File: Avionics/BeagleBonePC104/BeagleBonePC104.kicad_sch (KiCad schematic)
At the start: 0 parts

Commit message: Ian Goldberg - finished the pc104 pinout for the beaglebone motherboard
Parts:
- added U1: ~, symbol BeagleBoneBlackPinout:BeagleBoneBlackPinout
- added U2: ~, symbol PCI104:PCI104Connector
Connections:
- new net GND: U1.1 (GND), U1.2 (GND)
- new net UART5_RX: U2.35 (PLOD_STAT_3)
- new net UART5_TX: U2.33 (PLOD_STAT_1)

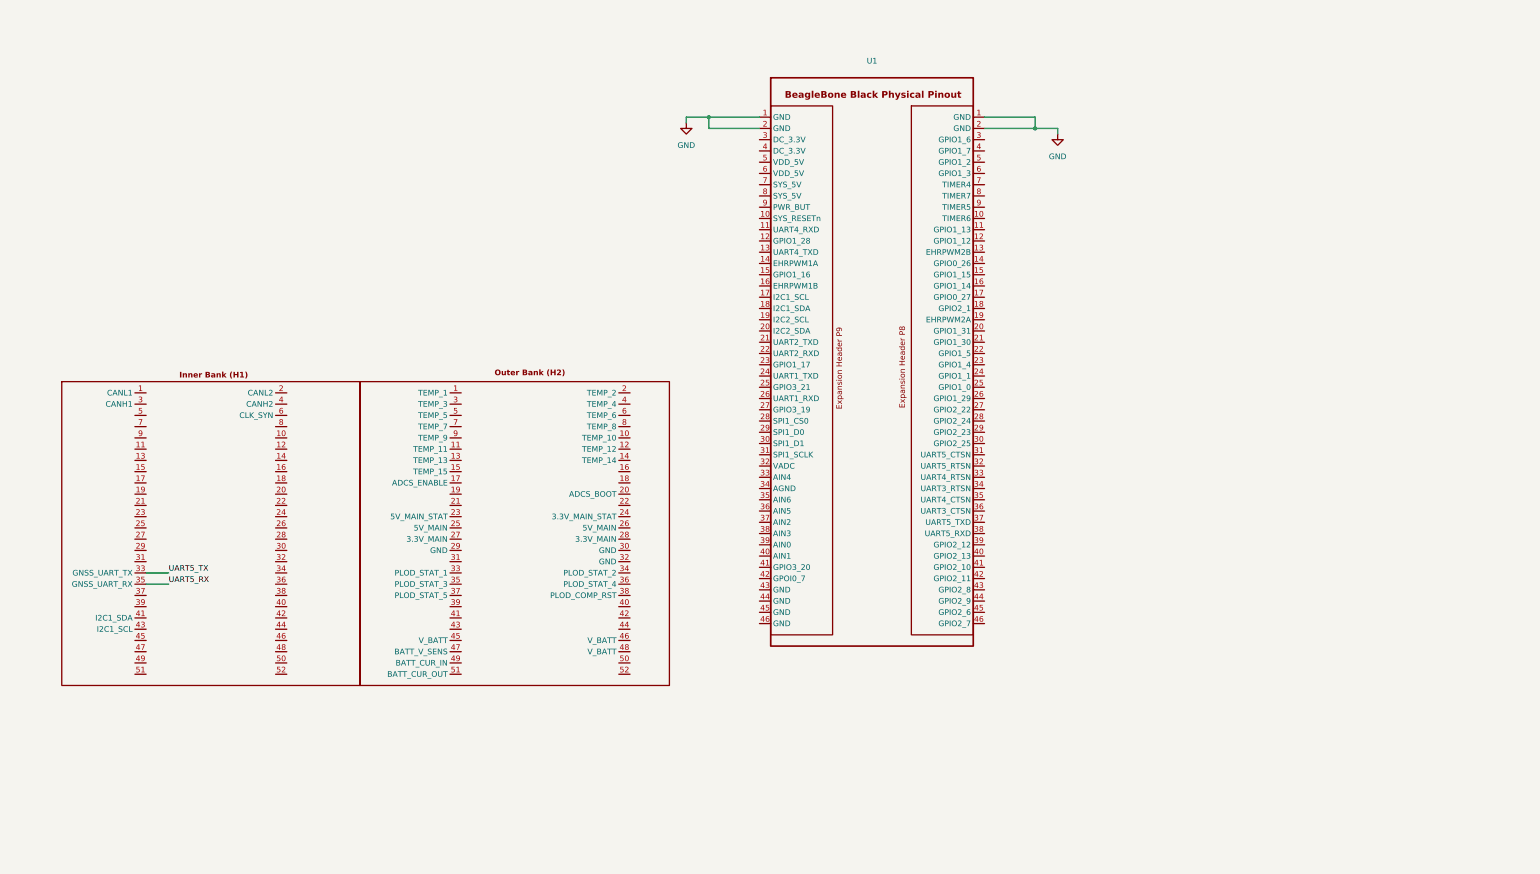
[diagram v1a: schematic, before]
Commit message: Ian Goldberg - Made more changes to the pc104 header for the BeagleBone
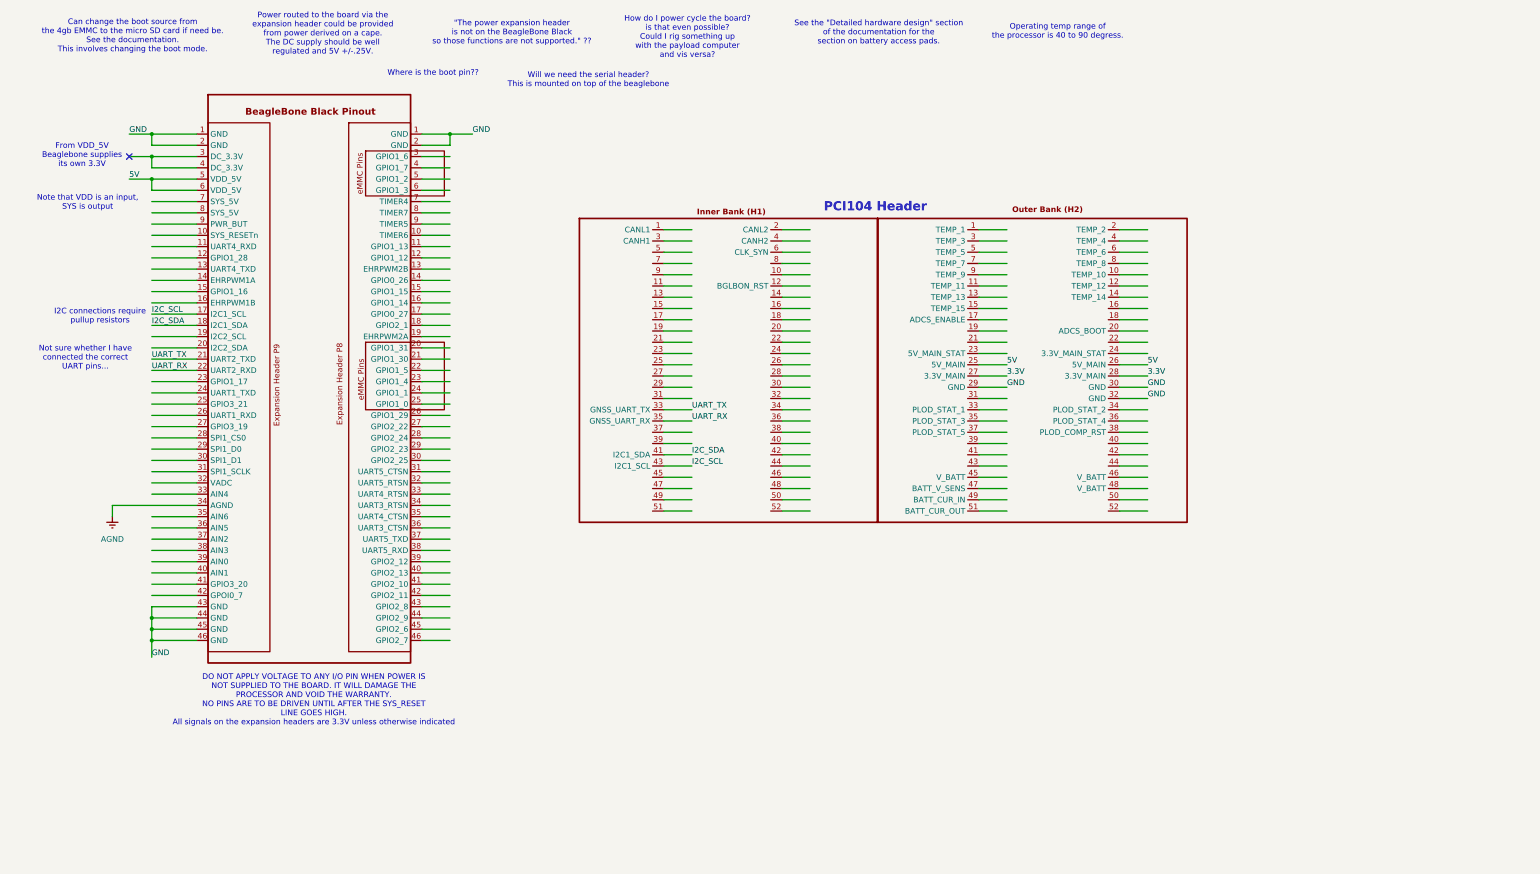
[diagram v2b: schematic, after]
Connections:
- net UART5_RX is gone; now on net UART_RX: U2.35 (PLOD_STAT_3)
- net UART5_TX is gone; now on net UART_TX: U2.33 (PLOD_STAT_1)
- net GND: now also U1.43 (GPIO2_8), U1.44 (GPIO2_9), U1.45 (GPIO2_6), U1.46 (GPIO2_7), U2.29 (GND), U2.30 (GND), U2.32 (GND)
- net I2C_SCL: now reaches U1.17 (I2C1_SCL)
- net I2C_SCL: now also U2.43 (I2C1_SCL)
- net I2C_SDA: now reaches U1.18 (I2C1_SDA)
- net I2C_SDA: now also U2.41 (I2C1_SDA)
- net UART_TX: now reaches U1.21 (UART2_TXD)
- net UART_RX: now reaches U1.22 (UART2_RXD)
- net at U1.3 (GPIO1_6): now also U1.4 (GPIO1_7)
- net AGND: now reaches U1.34 (UART3_RTSN)
- net 5V: now reaches U1.5 (VDD_5V)
- net 5V: now also U1.6 (VDD_5V), U2.25 (5V_MAIN), U2.26 (5V_MAIN)
- net 3.3V: now reaches U2.27 (3.3V_MAIN)
- net 3.3V: now also U2.28 (3.3V_MAIN)
- no-connect marks 0 -> 1
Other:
- note added: ""The power expansion header is not on the BeagleBone Black so those functions are not supported." ??"
- note added: "Can change the boot source from the 4gb EMMC to the micro SD card if need be. See the documentation. This involves changing the boot mode."
- note added: "DO NOT APPLY VOLTAGE TO ANY I/O PIN WHEN POWER IS NOT SUPPLIED TO THE BOARD. IT WILL DAMAGE THE PROCESSOR AND VOID THE WARRANTY. NO PINS ARE TO BE DRIVEN UNTIL AFTER THE SYS_RESET LINE GOES HIGH. All signals on the expansion headers are 3.3V unless otherwise indicated"
- note added: "From VDD_5V Beaglebone supplies its own 3.3V"
- note added: "How do I power cycle the board? is that even possible? Could I rig something up with the payload computer and vis versa?"
- note added: "I2C connections require pullup resistors"
- note added: "Not sure whether I have connected the correct UART pins..."
- note added: "Note that VDD is an input, SYS is output"
- note added: "Operating temp range of the processor is 40 to 90 degress."
- note added: "PCI104 Header"
- note added: "Power routed to the board via the expansion header could be provided from power derived on a cape. The DC supply should be well regulated and 5V +/-.25V."
- note added: "See the "Detailed hardware design" section of the documentation for the section on battery access pads."
- note added: "Where is the boot pin??"
- note added: "Will we need the serial header? This is mounted on top of the beaglebone"

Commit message: Ian Goldberg - Finished the pc104 pinout for the beaglebone motherboard
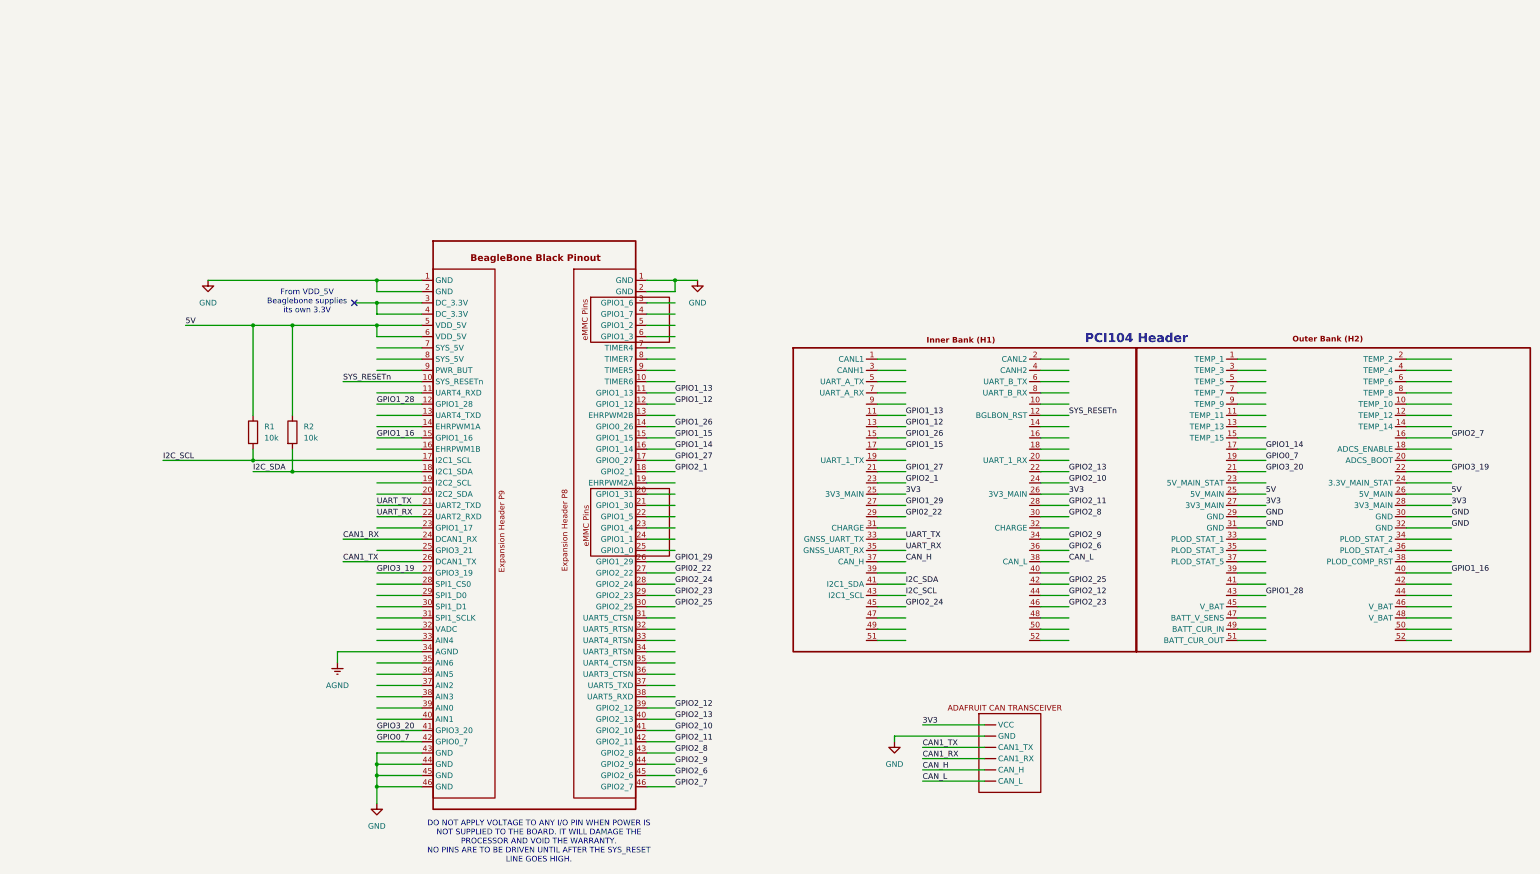
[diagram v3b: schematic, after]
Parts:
- added R1, R2: 10k, symbol Device:R
- added U3: ~, symbol BeagleBoneBlackPinout:AdafruitCANTransciever
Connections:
- net 5V: now also R1.1, R2.1
- net GND: now also U2.31 (GND), U3. (VCC)
- net I2C_SCL: now also R1.2
- net I2C_SDA: now also R2.2
- net SYS_RESETn: now reaches U1.10 (TIMER6)
- net SYS_RESETn: now also U2.12 (TEMP_12)
- net GPIO1_13: now reaches U1.11 (UART4_RXD)
- net GPIO1_13: now also U2.11 (TEMP_11)
- net GPIO1_28: now reaches U1.12 (GPIO1_28)
- net GPIO1_28: now also U2.43 (I2C1_SCL)
- net GPIO1_26: now reaches U1.14 (GPIO0_26)
- net GPIO1_26: now also U2.15 (TEMP_15)
- net GPIO1_16: now reaches U1.15 (GPIO1_16)
- net GPIO1_16: now also U2.40
- net GPIO1_14: now reaches U1.16 (GPIO1_14)
- net GPIO1_14: now also U2.17
- net CAN1_RX: now reaches U1.24 (GPIO1_1)
- net CAN1_RX: now also U3. (VCC)
- net GPIO1_29: now reaches U1.26 (GPIO1_29)
- net GPIO1_29: now also U2.27 (3V3_MAIN)
- net GPIO3_19: now reaches U1.27 (GPIO3_19)
- net GPIO3_19: now also U2.22
- net GPIO2_24: now reaches U1.28 (SPI1_CS0)
- net GPIO2_24: now also U2.45 (V_BAT)
- net GPIO2_23: now reaches U1.29 (SPI1_D0)
- net GPIO2_23: now also U2.46 (V_BAT)
- net at U1.3 (GPIO1_6): now also U1.4 (GPIO1_7)
- net at U1.4 (GPIO1_7): no longer U1.3 (GPIO1_6)
- net GPIO2_25: now reaches U1.30 (SPI1_D1)
- net GPIO2_25: now also U2.42
- net GPIO2_12: now reaches U1.39 (GPIO2_12)
- net GPIO2_12: now also U2.44
- net GPIO2_13: now reaches U1.40 (GPIO2_13)
- net GPIO2_13: now also U2.22
- net GPIO3_20: now reaches U1.41 (GPIO3_20)
- net GPIO3_20: now also U2.21
- net GPIO2_11: now reaches U1.42 (GPIO2_11)
- net GPIO2_11: now also U2.28 (3V3_MAIN)
- net GPIO2_8: now reaches U1.43 (GPIO2_8)
- net GPIO2_8: now also U2.30 (GND)
- net GPIO2_9: now reaches U1.44 (GPIO2_9)
- net GPIO2_9: now also U2.34 (PLOD_STAT_2)
- net GPIO2_6: now reaches U1.45 (GPIO2_6)
- net GPIO2_6: now also U2.36 (PLOD_STAT_4)
- net GPIO2_7: now reaches U1.46 (GPIO2_7)
- net GPIO2_7: now also U2.16
- net GPIO1_12: now reaches U2.13 (TEMP_13)
- net GPIO1_12: now also U1.12 (GPIO1_28)
- net GPIO1_15: now reaches U2.17
- net GPIO1_15: now also U1.15 (GPIO1_16)
- net GPIO0_7: now reaches U2.19 (UART_1_TX)
- net GPIO0_7: now also U1.42 (GPIO2_11)
- net GPIO2_1: now reaches U2.23 (5V_MAIN_STAT)
- net GPIO2_1: now also U1.18 (I2C1_SDA)
- net GPIO2_10: now reaches U2.24 (3.3V_MAIN_STAT)
- net GPIO2_10: now also U1.41 (GPIO3_20)
- net GPI02_22: now reaches U2.29 (GND)
- net GPI02_22: now also U1.27 (GPIO3_19)
- net CAN_H: now reaches U2.37 (PLOD_STAT_5)
- net CAN_H: now also U3. (VCC)
- net CAN_L: now reaches U2.38 (PLOD_COMP_RST)
- net CAN_L: now also U3. (VCC)
- removed net 3.3V: U2.27 (3.3V_MAIN), U2.28 (3.3V_MAIN)
- new net 3V3: U2.25 (5V_MAIN), U2.26 (5V_MAIN), U2.27 (3V3_MAIN), U2.28 (3V3_MAIN), U3. (VCC)
- new net CAN1_TX: U1.26 (GPIO1_29), U3. (VCC)
- new net GPIO1_27: U1.17 (I2C1_SCL), U2.21
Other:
- note added: "DO NOT APPLY VOLTAGE TO ANY I/O PIN WHEN POWER IS NOT SUPPLIED TO THE BOARD. IT WILL DAMAGE THE PROCESSOR AND VOID THE WARRANTY. NO PINS ARE TO BE DRIVEN UNTIL AFTER THE SYS_RESET LINE GOES HIGH."
- note removed: ""The power expansion header is not on the BeagleBone Black so those functions are not supported." ??"
- note removed: "Can change the boot source from the 4gb EMMC to the micro SD card if need be. See the documentation. This involves changing the boot mode."
- note removed: "DO NOT APPLY VOLTAGE TO ANY I/O PIN WHEN POWER IS NOT SUPPLIED TO THE BOARD. IT WILL DAMAGE THE PROCESSOR AND VOID THE WARRANTY. NO PINS ARE TO BE DRIVEN UNTIL AFTER THE SYS_RESET LINE GOES HIGH. All signals on the expansion headers are 3.3V unless otherwise indicated"
- note removed: "How do I power cycle the board? is that even possible? Could I rig something up with the payload computer and vis versa?"
- note removed: "I2C connections require pullup resistors"
- note removed: "Not sure whether I have connected the correct UART pins..."
- note removed: "Note that VDD is an input, SYS is output"
- note removed: "Operating temp range of the processor is 40 to 90 degress."
- note removed: "Power routed to the board via the expansion header could be provided from power derived on a cape. The DC supply should be well regulated and 5V +/-.25V."
- note removed: "See the "Detailed hardware design" section of the documentation for the section on battery access pads."
- note removed: "Where is the boot pin??"
- note removed: "Will we need the serial header? This is mounted on top of the beaglebone"

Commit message: Finally (tentatively) finished the schematic for the PCI104 header pin bank. Yay.
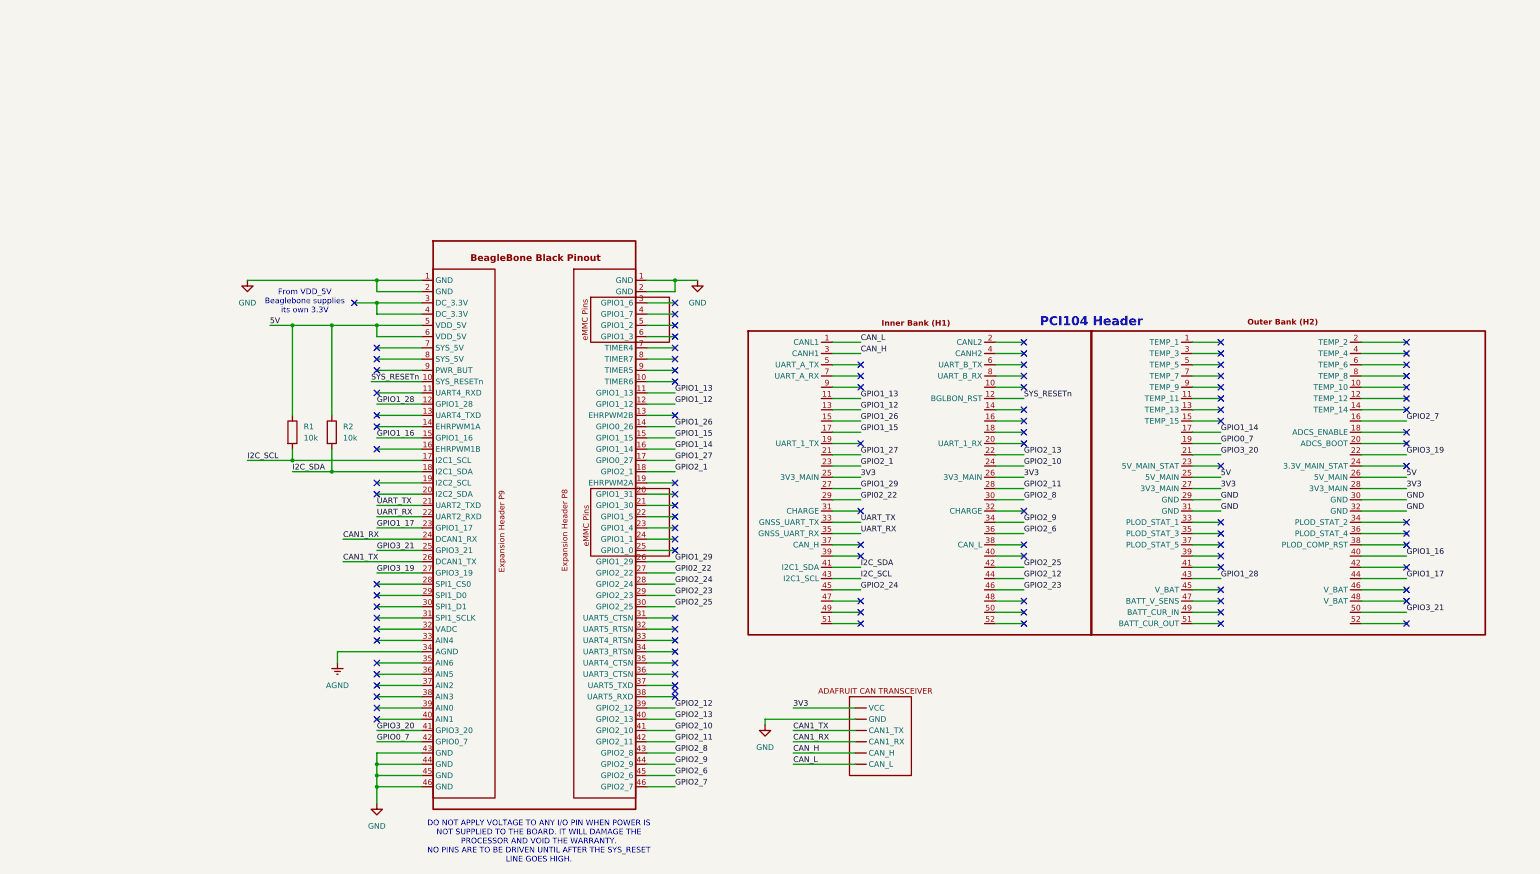
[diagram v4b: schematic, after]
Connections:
- net CAN_H: now also U2.3 (TEMP_3); no longer U2.37 (PLOD_STAT_5)
- net CAN_L: now also U2.1 (TEMP_1); no longer U2.38 (PLOD_COMP_RST)
- net GPIO1_17: now reaches U1.23 (GPIO1_4)
- net GPIO1_17: now also U2.44
- net GPIO3_21: now reaches U1.25 (GPIO3_21)
- net GPIO3_21: now also U2.50
- net at U1.3 (GPIO1_6): now also U1.4 (GPIO1_7)
- net at U1.4 (GPIO1_7): no longer U1.3 (GPIO1_6)
- no-connect marks 1 -> 107
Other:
- moved on the sheet: R1, R2

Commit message: Ian Goldberg - Almost finishes with the PC104 Layout,
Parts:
- R1, R2: footprint (none) -> Resistor_THT:R_Axial_DIN0207_L6.3mm_D2.5mm_P10.16mm_Horizontal
- U1: footprint (none) -> Module:BeagleBoneBlackFootprint
- U3: footprint (none) -> AdafruitCANTransciever:AdafruitCANPal_TJA1051T
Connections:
- net at U1.4 (GPIO1_7): no longer U1.3 (GPIO1_6)
- removed net AGND: U1.34 (UART3_RTSN)
- no-connect marks 107 -> 108
